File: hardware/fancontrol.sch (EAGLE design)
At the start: 13 parts, among them Q1 IRLZ44Z, T1 BC547

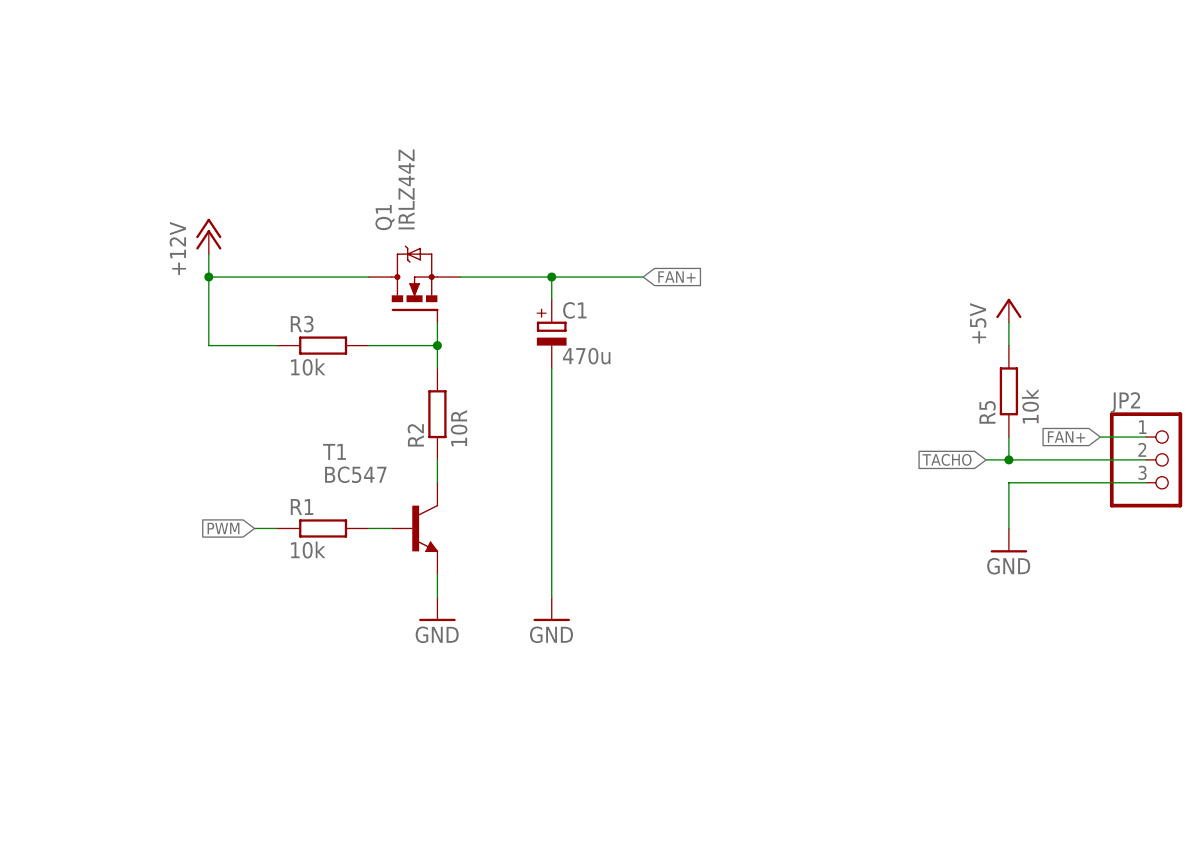
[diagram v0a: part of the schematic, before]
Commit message: New electronic
Changed the electronic design. Now only a transistor is needed, instead
of transistor and modfet.
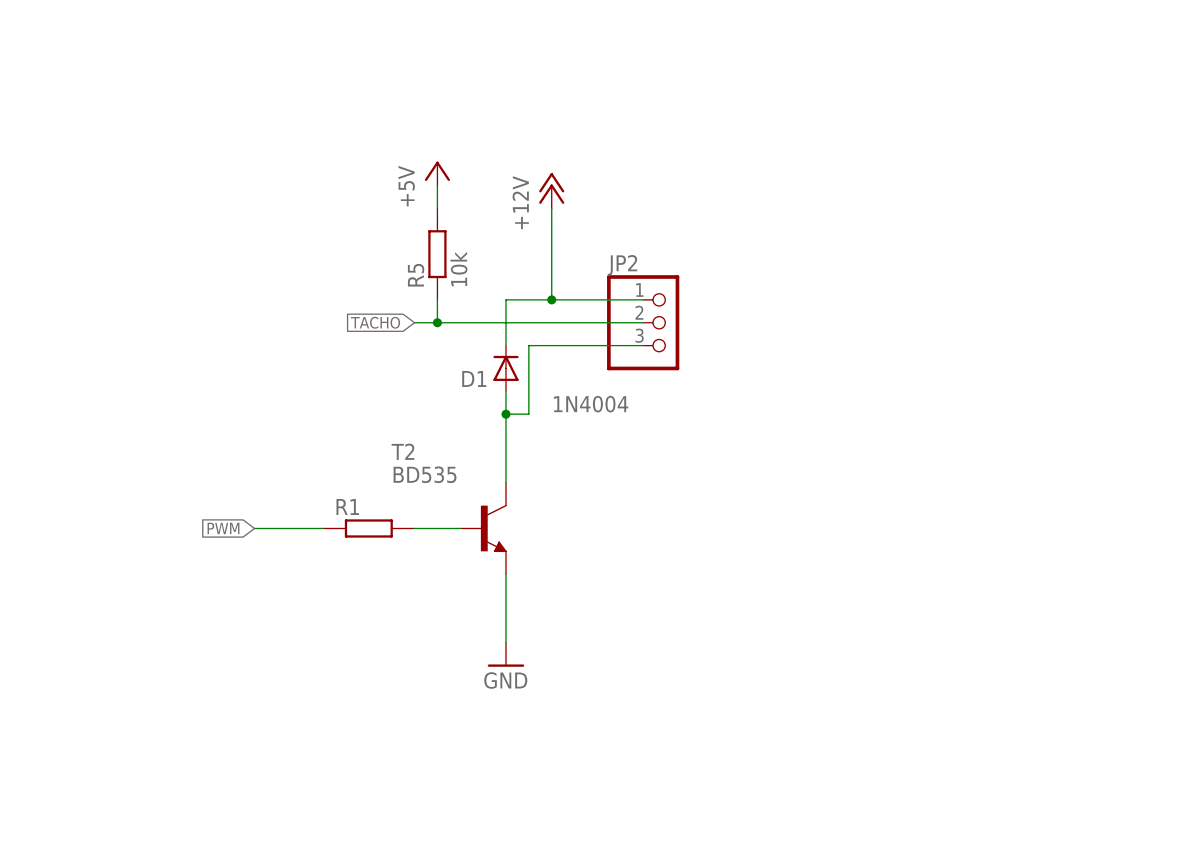
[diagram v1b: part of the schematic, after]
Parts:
- removed C1: 470u, rcl:CPOL-EUE5-10.5
- removed Q1: IRLZ44Z, transistor-power:IRLZ44Z
- removed R2: 10R, rcl:R-EU_0207/7
- removed R3: 10k, rcl:R-EU_0207/7
- removed T1: BC547, transistor:BC547
- added D1: 1N4004, diode:1N4004
- added T2: BD535, transistor:BD535
- R1: value 10k -> (none)
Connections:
- removed net FAN+: C1.+, JP2.1, Q1.S
- removed net N$3: Q1.G, R2.2, R3.2
- net +12V: now also D1.C, JP2.1; no longer Q1.D, R3.1
- net GND: now also T2.E; no longer C1.-, JP2.3, T1.E
- net N$1: now also D1.A, JP2.3, T2.C; no longer R1.2, T1.B
- net N$2: now also R1.2, T2.B; no longer R2.1, T1.C
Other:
- moved on the sheet: JP2, R1, R5
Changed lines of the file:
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@@
 <?xml version="1.0" encoding="utf-8"?>
 <!DOCTYPE eagle SYSTEM "eagle.dtd">
-<eagle version="6.4">
+<eagle version="6.2">
 <drawing>
 <settings>
@@
 <part name="P+2" library="supply1" deviceset="+12V" device=""/>
 <part name="GND1" library="supply1" deviceset="GND" device=""/>
-<part name="Q1" library="transistor-power" deviceset="IRLZ44Z" device=""/>
-<part name="R1" library="rcl" deviceset="R-EU_" device="0207/7" value="10k"/>
-<part name="T1" library="transistor" deviceset="BC547" device=""/>
-<part name="R2" library="rcl" deviceset="R-EU_" device="0207/7" value="10R"/>
-<part name="R3" library="rcl" deviceset="R-EU_" device="0207/7" value="10k"/>
-<part name="C1" library="rcl" deviceset="CPOL-EU" device="E5-10.5" value="470u"/>
-<part name="GND2" library="supply1" deviceset="GND" device=""/>
+<part name="R1" library="rcl" deviceset="R-EU_" device="0207/7"/>
 <part name="ARDUINO1" library="arduino" deviceset="ARDUINO" device=""/>
 <part name="GND3" library="supply1" deviceset="GND" device=""/>
@@
 <part name="P+3" library="supply1" deviceset="+12V" device=""/>
 <part name="JP2" library="pinhead" deviceset="PINHD-1X3" device=""/>
-<part name="GND5" library="supply1" deviceset="GND" device=""/>
 <part name="R5" library="rcl" deviceset="R-EU_" device="0207/7" value="10k"/>
 <part name="P+5" library="supply1" deviceset="+5V" device=""/>
@@
 <part name="GND6" library="supply1" deviceset="GND" device=""/>
 <part name="P+6" library="supply1" deviceset="+12V" device=""/>
+<part name="T2" library="transistor" deviceset="BD535" device=""/>
+<part name="D1" library="diode" deviceset="1N4004" device=""/>
 </parts>
 <sheets>
@@
 <instance part="FRAME1" gate="G$1" x="0" y="0"/>
 <instance part="FRAME1" gate="G$2" x="162.56" y="0"/>
-<instance part="P+2" gate="1" x="111.76" y="137.16"/>
-<instance part="GND1" gate="1" x="137.16" y="93.98"/>
-<instance part="Q1" gate="G$1" x="134.62" y="129.54" rot="R90"/>
-<instance part="R1" gate="G$1" x="124.46" y="104.14"/>
-<instance part="T1" gate="G$1" x="134.62" y="104.14"/>
-<instance part="R2" gate="G$1" x="137.16" y="116.84" rot="R90"/>
-<instance part="R3" gate="G$1" x="124.46" y="124.46"/>
-<instance part="C1" gate="G$1" x="149.86" y="127"/>
-<instance part="GND2" gate="1" x="149.86" y="93.98"/>
+<instance part="P+2" gate="1" x="149.86" y="142.24"/>
+<instance part="GND1" gate="1" x="144.78" y="88.9"/>
+<instance part="R1" gate="G$1" x="129.54" y="104.14"/>
 <instance part="ARDUINO1" gate="G$1" x="50.8" y="50.8"/>
 <instance part="GND3" gate="1" x="10.16" y="53.34"/>
@@
 </instance>
 <instance part="P+3" gate="1" x="5.08" y="91.44"/>
-<instance part="JP2" gate="A" x="218.44" y="111.76"/>
-<instance part="GND5" gate="1" x="200.66" y="101.6"/>
-<instance part="R5" gate="G$1" x="200.66" y="119.38" rot="R90"/>
-<instance part="P+5" gate="1" x="200.66" y="129.54"/>
+<instance part="JP2" gate="A" x="162.56" y="127"/>
+<instance part="R5" gate="G$1" x="137.16" y="134.62" rot="R90"/>
+<instance part="P+5" gate="1" x="137.16" y="144.78"/>
 <instance part="C2" gate="G$1" x="50.8" y="111.76"/>
 <instance part="C3" gate="G$1" x="58.42" y="111.76"/>
 <instance part="GND6" gate="1" x="50.8" y="99.06"/>
 <instance part="P+6" gate="1" x="50.8" y="121.92"/>
+<instance part="T2" gate="G$1" x="142.24" y="104.14"/>
+<instance part="D1" gate="1" x="144.78" y="121.92" smashed="yes" rot="R90">
+<attribute name="NAME" x="139.7" y="119.8626" size="1.778" layer="95"/>
+<attribute name="VALUE" x="149.86" y="117.0686" size="1.778" layer="96"/>
+</instance>
 </instances>
 <busses>
 </busses>
 <nets>
-<net name="N$1" class="0">
-<segment>
-<pinref part="R1" gate="G$1" pin="2"/>
-<pinref part="T1" gate="G$1" pin="B"/>
-<wire x1="129.54" y1="104.14" x2="132.08" y2="104.14" width="0.1524" layer="91"/>
-</segment>
-</net>
-<net name="N$2" class="0">
-<segment>
-<pinref part="R2" gate="G$1" pin="1"/>
-<pinref part="T1" gate="G$1" pin="C"/>
-<wire x1="137.16" y1="111.76" x2="137.16" y2="109.22" width="0.1524" layer="91"/>
-</segment>
-</net>
 <net name="GND" class="0">
-<segment>
-<pinref part="T1" gate="G$1" pin="E"/>
-<pinref part="GND1" gate="1" pin="GND"/>
-<wire x1="137.16" y1="99.06" x2="137.16" y2="96.52" width="0.1524" layer="91"/>
-</segment>
-<segment>
-<pinref part="C1" gate="G$1" pin="-"/>
-<pinref part="GND2" gate="1" pin="GND"/>
-<wire x1="149.86" y1="121.92" x2="149.86" y2="96.52" width="0.1524" layer="91"/>
-</segment>
 <segment>
 <pinref part="ARDUINO1" gate="G$1" pin="GND"/>
@@
 <wire x1="45.72" y1="144.78" x2="55.88" y2="144.78" width="0.1524" layer="91"/>
 <wire x1="55.88" y1="144.78" x2="55.88" y2="137.16" width="0.1524" layer="91"/>
-</segment>
-<segment>
-<pinref part="JP2" gate="A" pin="3"/>
-<pinref part="GND5" gate="1" pin="GND"/>
-<wire x1="215.9" y1="109.22" x2="200.66" y2="109.22" width="0.1524" layer="91"/>
-<wire x1="200.66" y1="109.22" x2="200.66" y2="104.14" width="0.1524" layer="91"/>
 </segment>
 <segment>
@@
 <junction x="50.8" y="104.14"/>
 </segment>
-</net>
-<net name="N$3" class="0">
-<segment>
-<pinref part="R2" gate="G$1" pin="2"/>
-<pinref part="Q1" gate="G$1" pin="G"/>
-<wire x1="137.16" y1="121.92" x2="137.16" y2="124.46" width="0.1524" layer="91"/>
-<pinref part="R3" gate="G$1" pin="2"/>
-<wire x1="137.16" y1="124.46" x2="137.16" y2="127" width="0.1524" layer="91"/>
-<wire x1="129.54" y1="124.46" x2="137.16" y2="124.46" width="0.1524" layer="91"/>
-<junction x="137.16" y="124.46"/>
+<segment>
+<pinref part="T2" gate="G$1" pin="E"/>
+<wire x1="144.78" y1="99.06" x2="144.78" y2="91.44" width="0.1524" layer="91"/>
+<pinref part="GND1" gate="1" pin="GND"/>
 </segment>
 </net>
 <net name="+12V" class="0">
-<segment>
-<pinref part="Q1" gate="G$1" pin="D"/>
-<pinref part="P+2" gate="1" pin="+12V"/>
-<wire x1="129.54" y1="132.08" x2="111.76" y2="132.08" width="0.1524" layer="91"/>
-<wire x1="111.76" y1="132.08" x2="111.76" y2="134.62" width="0.1524" layer="91"/>
-<pinref part="R3" gate="G$1" pin="1"/>
-<wire x1="119.38" y1="124.46" x2="111.76" y2="124.46" width="0.1524" layer="91"/>
-<wire x1="111.76" y1="124.46" x2="111.76" y2="132.08" width="0.1524" layer="91"/>
-<junction x="111.76" y="132.08"/>
-</segment>
 <segment>
 <pinref part="ARDUINO1" gate="G$1" pin="VIN"/>
@@
 <pinref part="P+6" gate="1" pin="+12V"/>
 </segment>
-</net>
-<net name="FAN+" class="0">
-<segment>
-<pinref part="Q1" gate="G$1" pin="S"/>
-<pinref part="C1" gate="G$1" pin="+"/>
-<wire x1="139.7" y1="132.08" x2="149.86" y2="132.08" width="0.1524" layer="91"/>
-<wire x1="149.86" y1="132.08" x2="149.86" y2="129.54" width="0.1524" layer="91"/>
-<wire x1="149.86" y1="132.08" x2="160.02" y2="132.08" width="0.1524" layer="91"/>
-<junction x="149.86" y="132.08"/>
-<label x="160.02" y="132.08" size="1.27" layer="95" xref="yes"/>
-</segment>
 <segment>
 <pinref part="JP2" gate="A" pin="1"/>
-<wire x1="215.9" y1="114.3" x2="210.82" y2="114.3" width="0.1524" layer="91"/>
-<label x="210.82" y="114.3" size="1.27" layer="95" rot="R180" xref="yes"/>
+<pinref part="P+2" gate="1" pin="+12V"/>
+<wire x1="160.02" y1="129.54" x2="149.86" y2="129.54" width="0.1524" layer="91"/>
+<wire x1="149.86" y1="129.54" x2="149.86" y2="139.7" width="0.1524" layer="91"/>
+<pinref part="D1" gate="1" pin="C"/>
+<wire x1="149.86" y1="129.54" x2="144.78" y2="129.54" width="0.1524" layer="91"/>
+<wire x1="144.78" y1="129.54" x2="144.78" y2="124.46" width="0.1524" layer="91"/>
+<junction x="149.86" y="129.54"/>
 </segment>
 </net>
@@
 <pinref part="P+5" gate="1" pin="+5V"/>
 <pinref part="R5" gate="G$1" pin="2"/>
-<wire x1="200.66" y1="127" x2="200.66" y2="124.46" width="0.1524" layer="91"/>
+<wire x1="137.16" y1="142.24" x2="137.16" y2="139.7" width="0.1524" layer="91"/>
 </segment>
 </net>
@@
 <segment>
 <pinref part="JP2" gate="A" pin="2"/>
-<wire x1="215.9" y1="111.76" x2="200.66" y2="111.76" width="0.1524" layer="91"/>
+<wire x1="160.02" y1="127" x2="137.16" y2="127" width="0.1524" layer="91"/>
 <pinref part="R5" gate="G$1" pin="1"/>
-<wire x1="200.66" y1="114.3" x2="200.66" y2="111.76" width="0.1524" layer="91"/>
-<wire x1="200.66" y1="111.76" x2="198.12" y2="111.76" width="0.1524" layer="91"/>
-<junction x="200.66" y="111.76"/>
-<label x="198.12" y="111.76" size="1.27" layer="95" rot="R180" xref="yes"/>
+<wire x1="137.16" y1="129.54" x2="137.16" y2="127" width="0.1524" layer="91"/>
+<wire x1="137.16" y1="127" x2="134.62" y2="127" width="0.1524" layer="91"/>
+<junction x="137.16" y="127"/>
+<label x="134.62" y="127" size="1.27" layer="95" rot="R180" xref="yes"/>
 </segment>
 </net>
@@
 <segment>
 <pinref part="R1" gate="G$1" pin="1"/>
-<wire x1="119.38" y1="104.14" x2="116.84" y2="104.14" width="0.1524" layer="91"/>
+<wire x1="124.46" y1="104.14" x2="116.84" y2="104.14" width="0.1524" layer="91"/>
 <label x="116.84" y="104.14" size="1.27" layer="95" rot="R180" xref="yes"/>
 </segment>
 </net>
+<net name="N$1" class="0">
+<segment>
+<pinref part="JP2" gate="A" pin="3"/>
+<wire x1="160.02" y1="124.46" x2="147.32" y2="124.46" width="0.1524" layer="91"/>
+<wire x1="147.32" y1="124.46" x2="147.32" y2="116.84" width="0.1524" layer="91"/>
+<pinref part="T2" gate="G$1" pin="C"/>
+<wire x1="147.32" y1="116.84" x2="144.78" y2="116.84" width="0.1524" layer="91"/>
+<wire x1="144.78" y1="116.84" x2="144.78" y2="109.22" width="0.1524" layer="91"/>
+<pinref part="D1" gate="1" pin="A"/>
+<wire x1="144.78" y1="119.38" x2="144.78" y2="116.84" width="0.1524" layer="91"/>
+<junction x="144.78" y="116.84"/>
+</segment>
+</net>
+<net name="N$2" class="0">
+<segment>
+<pinref part="T2" gate="G$1" pin="B"/>
+<pinref part="R1" gate="G$1" pin="2"/>
+<wire x1="139.7" y1="104.14" x2="134.62" y2="104.14" width="0.1524" layer="91"/>
+</segment>
+</net>
